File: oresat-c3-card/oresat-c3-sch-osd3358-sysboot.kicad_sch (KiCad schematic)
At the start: 26 parts, among them J6 Conn_01x02, Q2 DMN3028LQ-7, U1 OSD3358-1G-ISM, U39 TCAN330

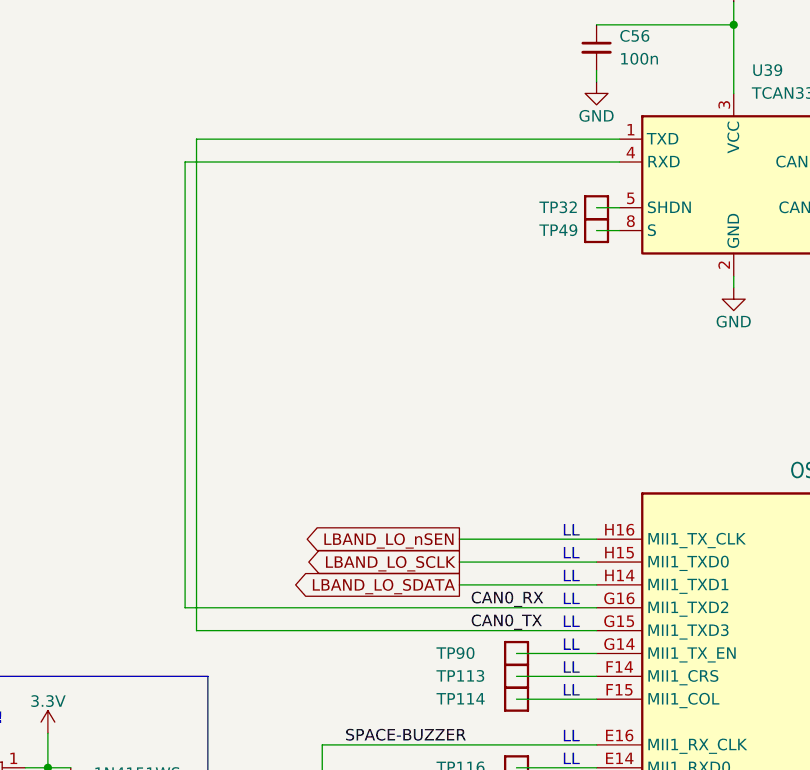
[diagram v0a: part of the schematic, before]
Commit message: Added L band ground cut (Glenn's fault). DRC errrors due to 50 ohm clearance; investigating custom rules now.
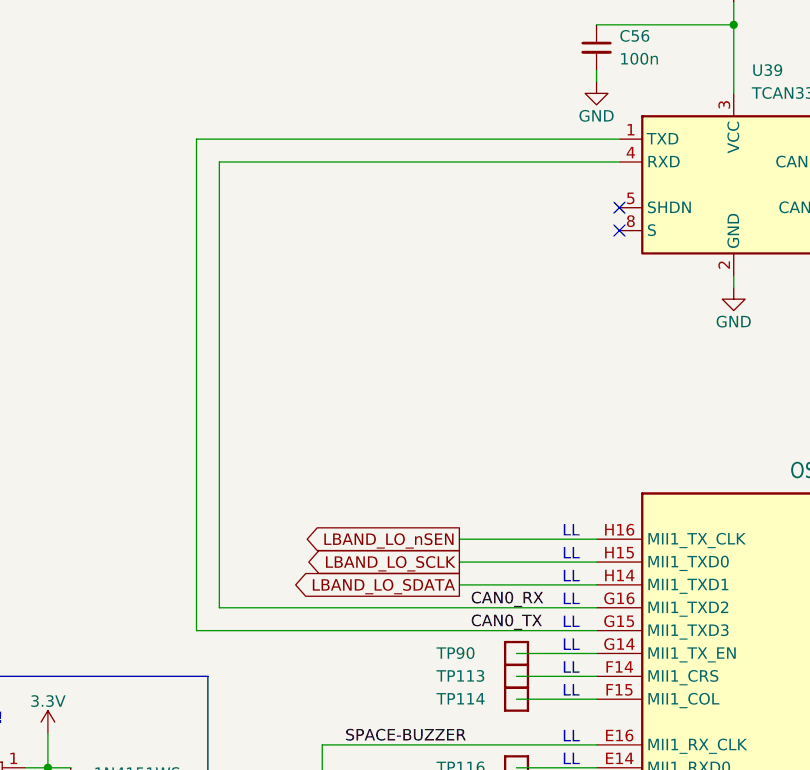
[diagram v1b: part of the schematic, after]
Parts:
- removed TP32, TP49: Test-Point, oresat-misc:TestPoint_Pad_D1.0mm, symbol oresat-misc:Test-Point-1mm-round
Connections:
- no-connect marks 8 -> 10
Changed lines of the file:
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@@
 	)
 	(no_connect
+		(at 161.29 91.44)
+	)
+	(no_connect
 		(at 280.67 171.45)
 	)
@@
 		(at 295.91 171.45)
 	)
+	(no_connect
+		(at 161.29 93.98)
+	)
 	(wire
 		(pts
@@
 	(wire
 		(pts
-			(xy 158.75 93.98) (xy 161.29 93.98)
-		)
-		(stroke
-			(width 0)
-			(type default)
-		)
-	)
-	(wire
-		(pts
 			(xy 265.43 119.38) (xy 265.43 135.89)
 		)
@@
 	(wire
 		(pts
-			(xy 113.03 86.36) (xy 161.29 86.36)
-		)
-		(stroke
-			(width 0)
-			(type default)
-		)
-	)
-	(wire
-		(pts
-			(xy 158.75 91.44) (xy 161.29 91.44)
+			(xy 116.84 86.36) (xy 161.29 86.36)
 		)
 		(stroke
@@
 	(wire
 		(pts
-			(xy 113.03 135.89) (xy 158.75 135.89)
+			(xy 116.84 135.89) (xy 158.75 135.89)
 		)
 		(stroke
@@
 	(wire
 		(pts
-			(xy 113.03 86.36) (xy 113.03 135.89)
+			(xy 116.84 86.36) (xy 116.84 135.89)
 		)
 		(stroke
@@
 	(symbol
 		(lib_id "oresat-misc:Test-Point-1mm-round")
-		(at 158.75 91.44 0)
-		(unit 1)
-		(exclude_from_sim yes)
-		(in_bom no)
-		(on_board yes)
-		(dnp no)
-		(property "Reference" "TP32"
-			(at 152.4 91.44 0)
-			(effects
-				(font
-					(size 1.27 1.27)
-				)
-				(justify left)
-			)
-		)
-		(property "Value" "Test-Point"
-			(at 158.75 88.9 0)
-			(effects
-				(font
-					(size 1.27 1.27)
-				)
-				(hide yes)
-			)
-		)
-		(property "Footprint" "oresat-misc:TestPoint_Pad_D1.0mm"
-			(at 158.75 81.28 0)
-			(effects
-				(font
-					(size 1.27 1.27)
-				)
-				(hide yes)
-			)
-		)
-		(property "Datasheet" ""
-			(at 158.75 91.44 0)
-			(effects
-				(font
-					(size 1.27 1.27)
-				)
-				(hide yes)
-			)
-		)
-		(property "Description" "1mm round SMT test point"
-			(at 158.75 91.44 0)
-			(effects
-				(font
-					(size 1.27 1.27)
-				)
-				(hide yes)
-			)
-		)
-		(pin "1"
-		)
-		(instances
-			(project "oresat-c3"
-				(path "/65d12cdd-c326-4033-9053-c59fa4e0b25e/0c732c1e-ab0d-41ac-9d77-9d7763333b6f"
-					(reference "TP32")
-					(unit 1)
-				)
-			)
-		)
-	)
-	(symbol
-		(lib_id "oresat-misc:Test-Point-1mm-round")
 		(at 149.86 166.37 270)
 		(unit 1)
@@
 				)
 			)
-		)
-	)
-	(symbol
-		(lib_id "oresat-misc:Test-Point-1mm-round")
-		(at 158.75 93.98 0)
-		(unit 1)
-		(exclude_from_sim yes)
-		(in_bom no)
-		(on_board yes)
-		(dnp no)
-		(property "Reference" "TP49"
-			(at 152.4 93.98 0)
-			(effects
-				(font
-					(size 1.27 1.27)
-				)
-				(justify left)
-			)
-		)
-		(property "Value" "Test-Point"
-			(at 158.75 91.44 0)
-			(effects
-				(font
-					(size 1.27 1.27)
-				)
-				(hide yes)
-			)
-		)
-		(property "Footprint" "oresat-misc:TestPoint_Pad_D1.0mm"
-			(at 158.75 83.82 0)
-			(effects
-				(font
-					(size 1.27 1.27)
-				)
-				(hide yes)
-			)
-		)
-		(property "Datasheet" ""
-			(at 158.75 93.98 0)
-			(effects
-				(font
-					(size 1.27 1.27)
-				)
-				(hide yes)
-			)
-		)
-		(property "Description" "1mm round SMT test point"
-			(at 158.75 93.98 0)
-			(effects
-				(font
-					(size 1.27 1.27)
-				)
-				(hide yes)
-			)
-		)
-		(pin "1"
-		)
-		(instances
-			(project "oresat-c3"
-				(path "/65d12cdd-c326-4033-9053-c59fa4e0b25e/0c732c1e-ab0d-41ac-9d77-9d7763333b6f"
-					(reference "TP49")
-					(unit 1)
-				)
-			)

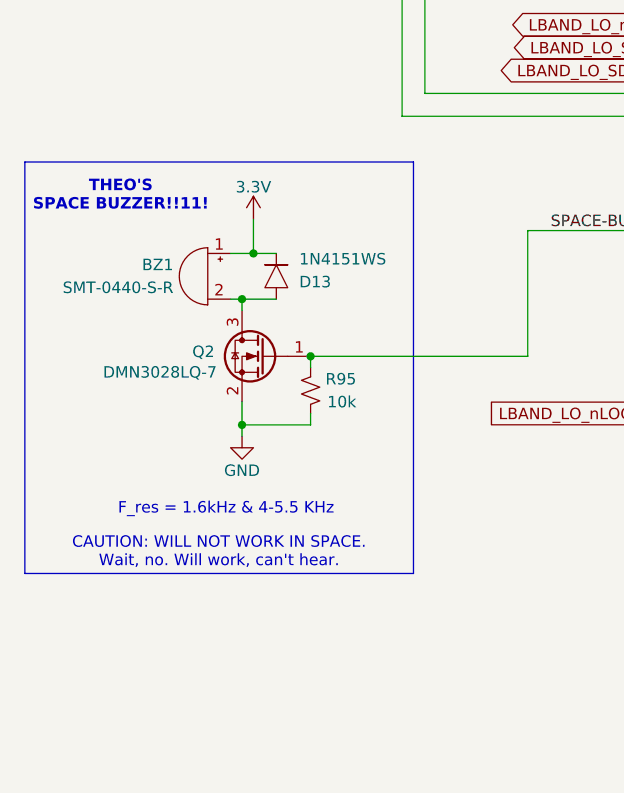
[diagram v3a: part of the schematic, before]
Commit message: Officially moving to C3 v7.1 with fixes based on the 7.0 and improvements from using the 7.0
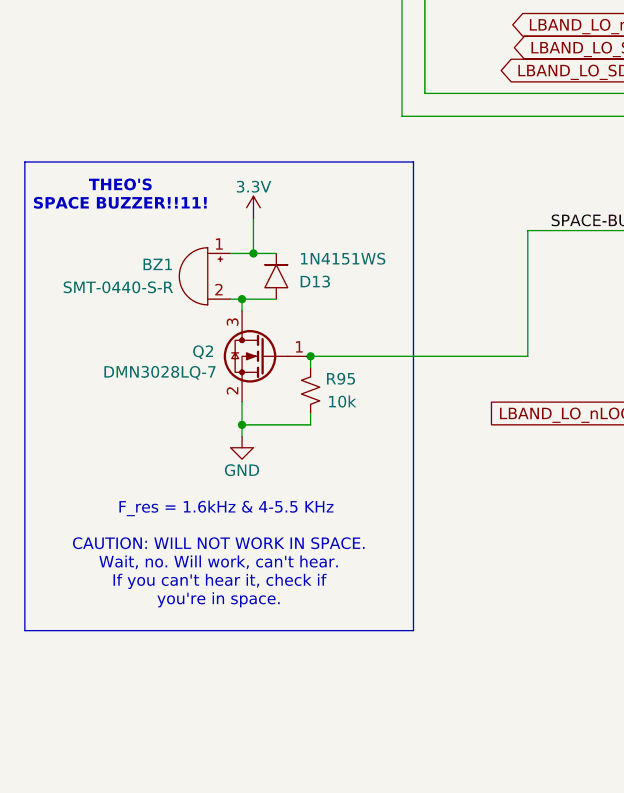
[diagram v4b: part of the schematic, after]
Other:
- note added: "CAUTION: WILL NOT WORK IN SPACE. Wait, no. Will work, can't hear. If you can't hear it, check if you're in space."
- note removed: "CAUTION: WILL NOT WORK IN SPACE. Wait, no. Will work, can't hear."
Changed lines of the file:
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@@
 	(title_block
 		(title "OreSat C3 Card")
-		(date "2026-03-20")
-		(rev "7.0")
+		(date "2026-06-07")
+		(rev "7.1")
 		(company "Portland State Aerospace Society")
 	)
 	(rectangle
 		(start 72.39 143.51)
-		(end 115.57 189.23)
+		(end 115.57 195.58)
 		(stroke
 			(width 0)
@@
 		)
 	)
-	(text "CAUTION: WILL NOT WORK IN SPACE.\nWait, no. Will work, can't hear."
-		(exclude_from_sim no)
-		(at 93.98 186.944 0)
-		(effects
-			(font
+	(text "CAUTION: WILL NOT WORK IN SPACE.\nWait, no. Will work, can't hear.\nIf you can't hear it, check if\nyou're in space."
+		(exclude_from_sim no)
+		(at 93.98 189.23 0)
+		(effects
+			(font
